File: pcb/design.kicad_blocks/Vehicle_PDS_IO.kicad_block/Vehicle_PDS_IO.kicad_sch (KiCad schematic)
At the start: 1 part, among them J10 FFC2B28-24-G

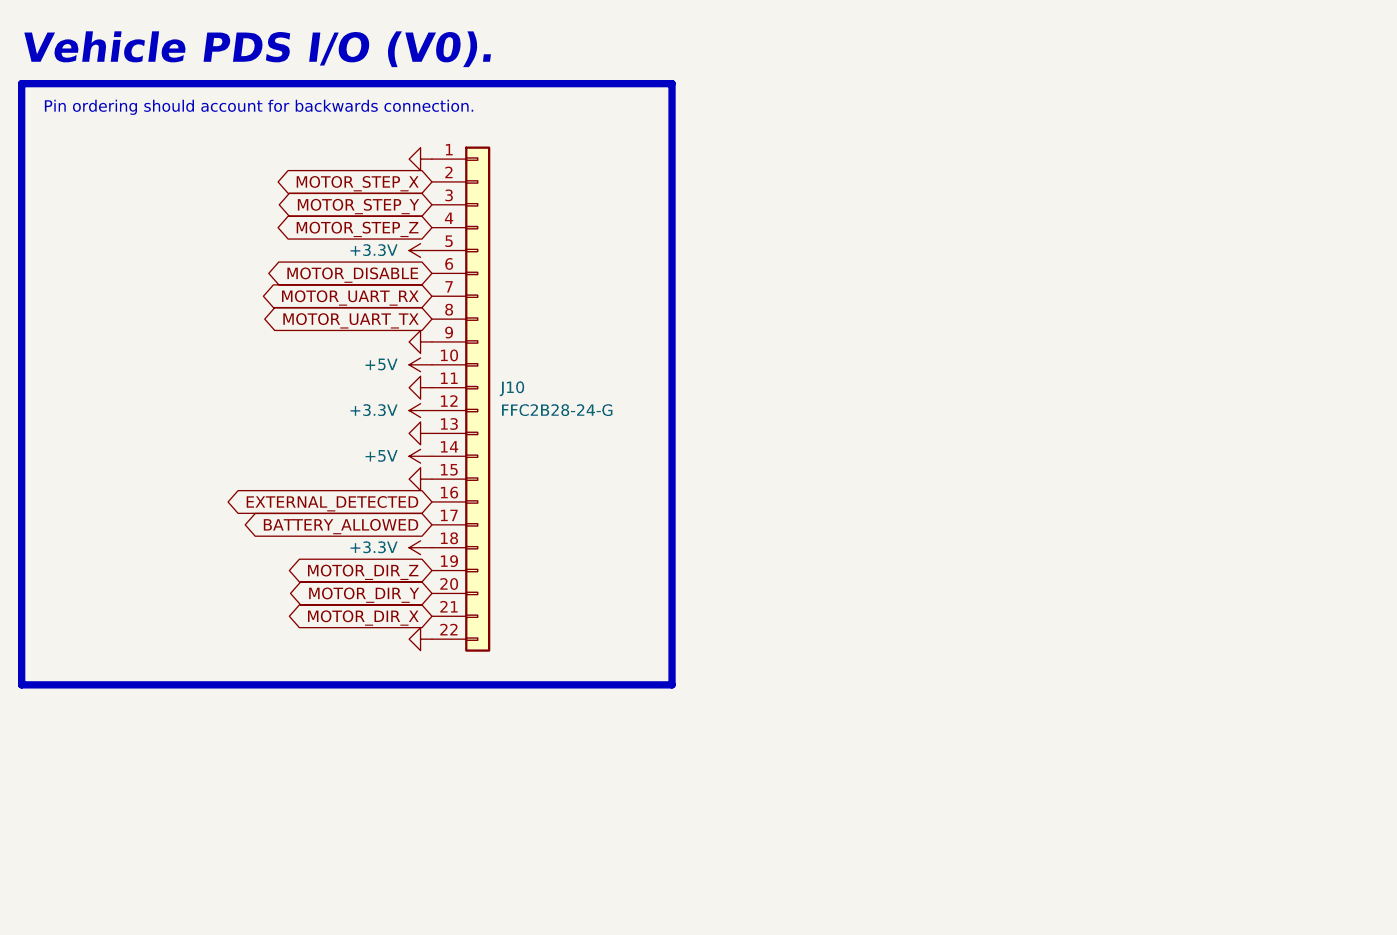
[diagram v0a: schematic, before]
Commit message: `Vehicle PDS I/O (V1 : Fixed pin-count).`
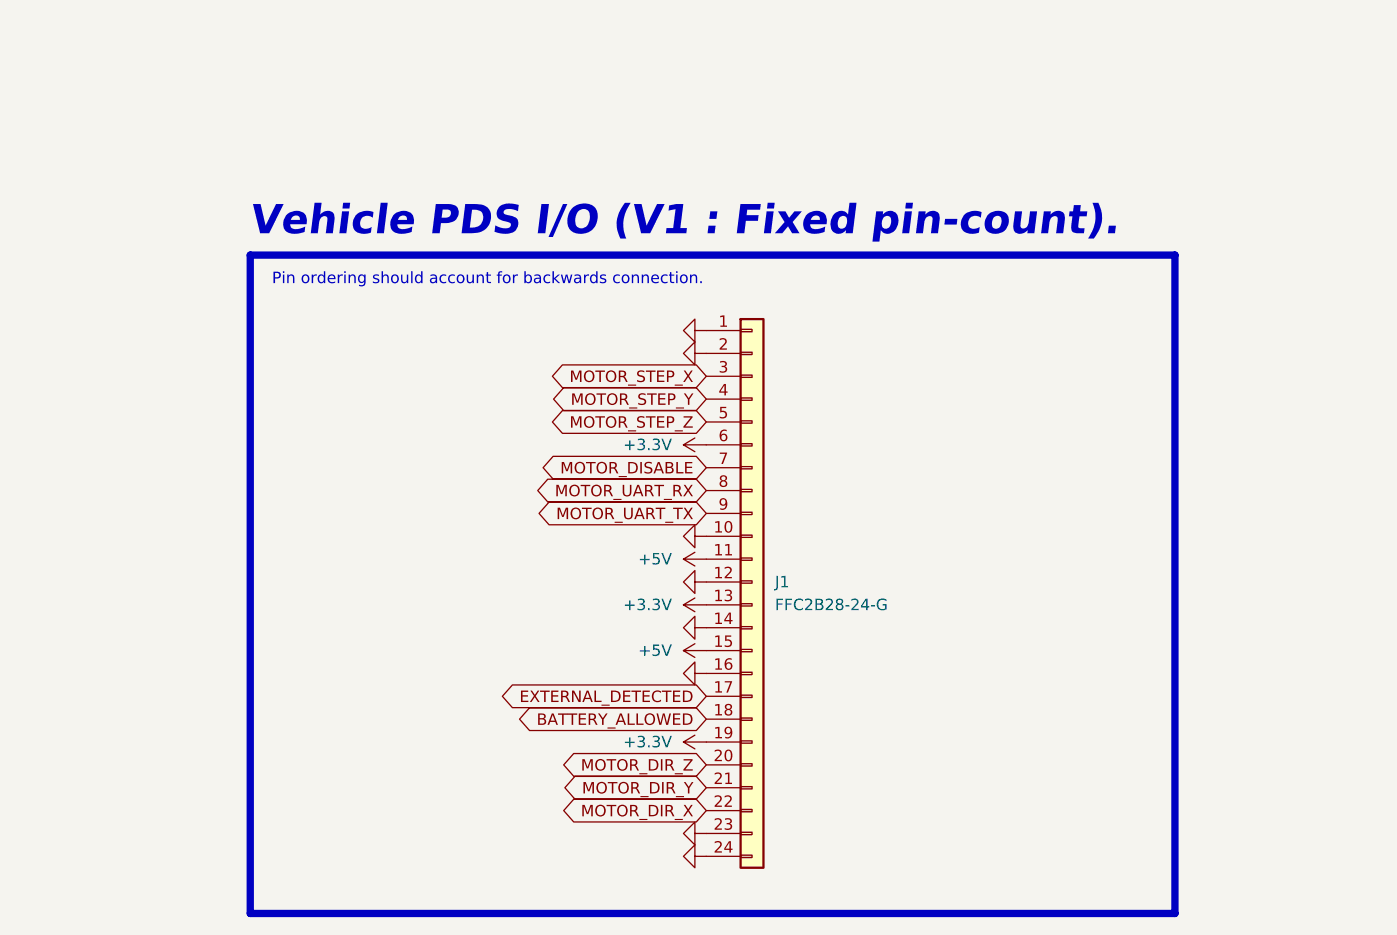
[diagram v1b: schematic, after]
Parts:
- J1: renamed from J10; symbol Connector_Generic:Conn_01x22 -> Connector_Generic:Conn_01x24
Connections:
- net +3.3V: now also J1.13 (Pin_13), J1.19 (Pin_19), J1.6 (Pin_6); no longer J1.12 (Pin_12), J1.18 (Pin_18), J1.5 (Pin_5)
- net +5V: now also J1.11 (Pin_11), J1.15 (Pin_15); no longer J1.10 (Pin_10), J1.14 (Pin_14)
- net BATTERY_ALLOWED: now also J1.18 (Pin_18); no longer J1.17 (Pin_17)
- net EXTERNAL_DETECTED: now also J1.17 (Pin_17); no longer J1.16 (Pin_16)
- net GND: now also J1.10 (Pin_10), J1.12 (Pin_12), J1.14 (Pin_14), J1.16 (Pin_16), J1.2 (Pin_2), J1.23 (Pin_23), J1.24 (Pin_24); no longer J1.11 (Pin_11), J1.13 (Pin_13), J1.15 (Pin_15), J1.22 (Pin_22), J1.9 (Pin_9)
- net MOTOR_DIR_X: now also J1.22 (Pin_22); no longer J1.21 (Pin_21)
- net MOTOR_DIR_Y: now also J1.21 (Pin_21); no longer J1.20 (Pin_20)
- net MOTOR_DIR_Z: now also J1.20 (Pin_20); no longer J1.19 (Pin_19)
- net MOTOR_DISABLE: now also J1.7 (Pin_7); no longer J1.6 (Pin_6)
- net MOTOR_STEP_X: now also J1.3 (Pin_3); no longer J1.2 (Pin_2)
- net MOTOR_STEP_Y: now also J1.4 (Pin_4); no longer J1.3 (Pin_3)
- net MOTOR_STEP_Z: now also J1.5 (Pin_5); no longer J1.4 (Pin_4)
- net MOTOR_UART_RX: now also J1.8 (Pin_8); no longer J1.7 (Pin_7)
- net MOTOR_UART_TX: now also J1.9 (Pin_9); no longer J1.8 (Pin_8)
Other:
- note added: "Vehicle PDS I/O (V1 : Fixed pin-count)."
- note removed: "Vehicle PDS I/O (V0)."

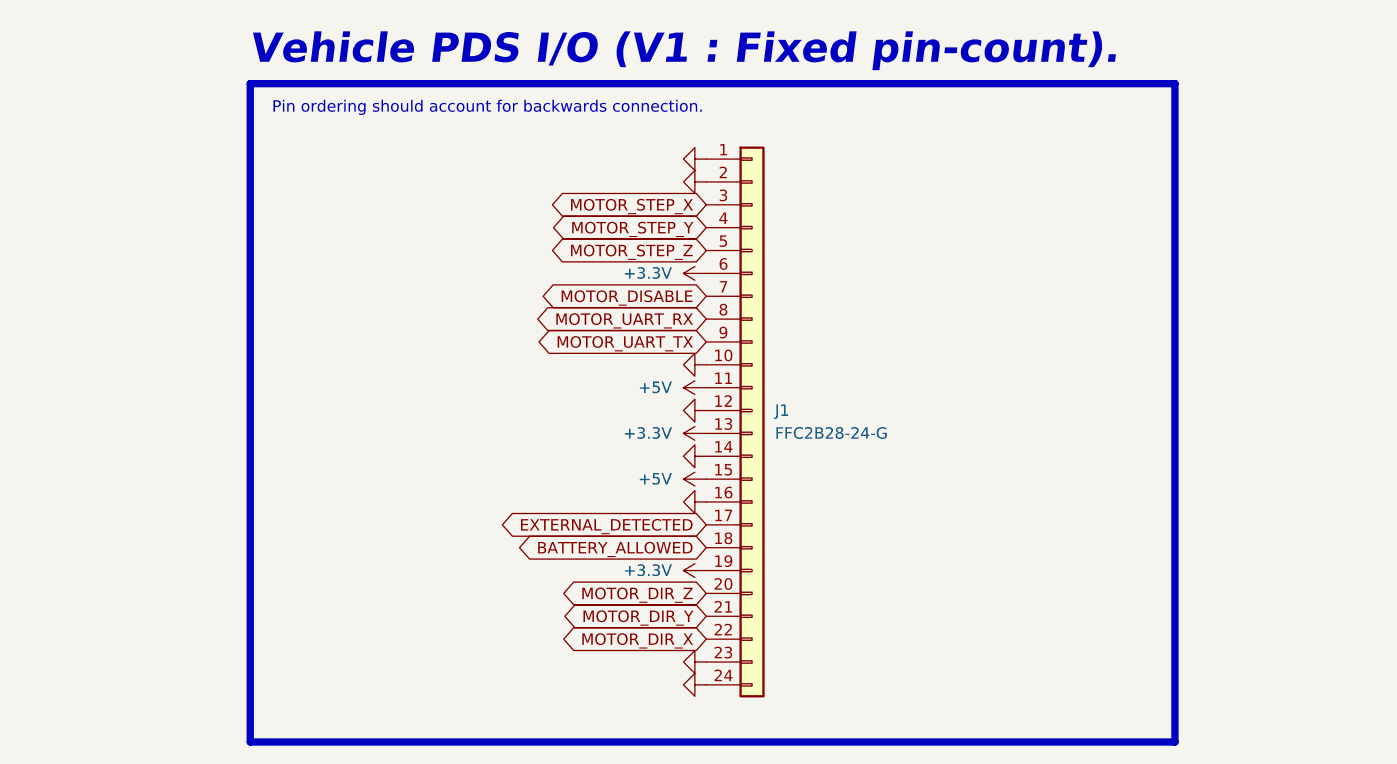
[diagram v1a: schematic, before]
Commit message: Made `VehicleFlightComputer` target and corrected nets for the STM32H533VET6 on `VehicleFlightComputer` PCB.
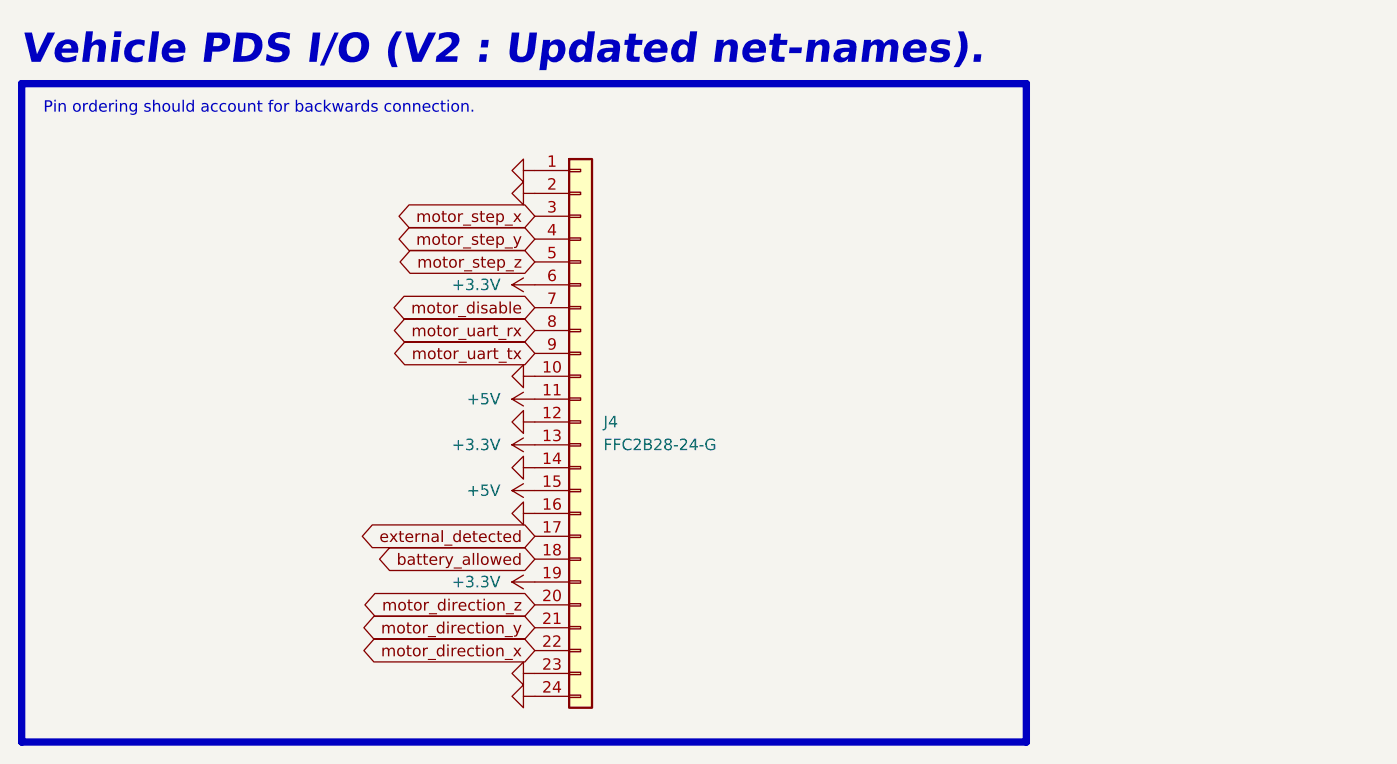
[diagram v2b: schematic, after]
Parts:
- renumbered J1 to J4
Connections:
- net BATTERY_ALLOWED renamed battery_allowed
- net EXTERNAL_DETECTED renamed external_detected
- net MOTOR_DIR_X renamed motor_direction_x
- net MOTOR_DIR_Y renamed motor_direction_y
- net MOTOR_DIR_Z renamed motor_direction_z
- net MOTOR_DISABLE renamed motor_disable
- net MOTOR_STEP_X renamed motor_step_x
- net MOTOR_STEP_Y renamed motor_step_y
- net MOTOR_STEP_Z renamed motor_step_z
- net MOTOR_UART_RX renamed motor_uart_rx
- net MOTOR_UART_TX renamed motor_uart_tx
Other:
- note added: "Vehicle PDS I/O (V2 : Updated net-names)."
- note removed: "Vehicle PDS I/O (V1 : Fixed pin-count)."
- moved on the sheet: J4

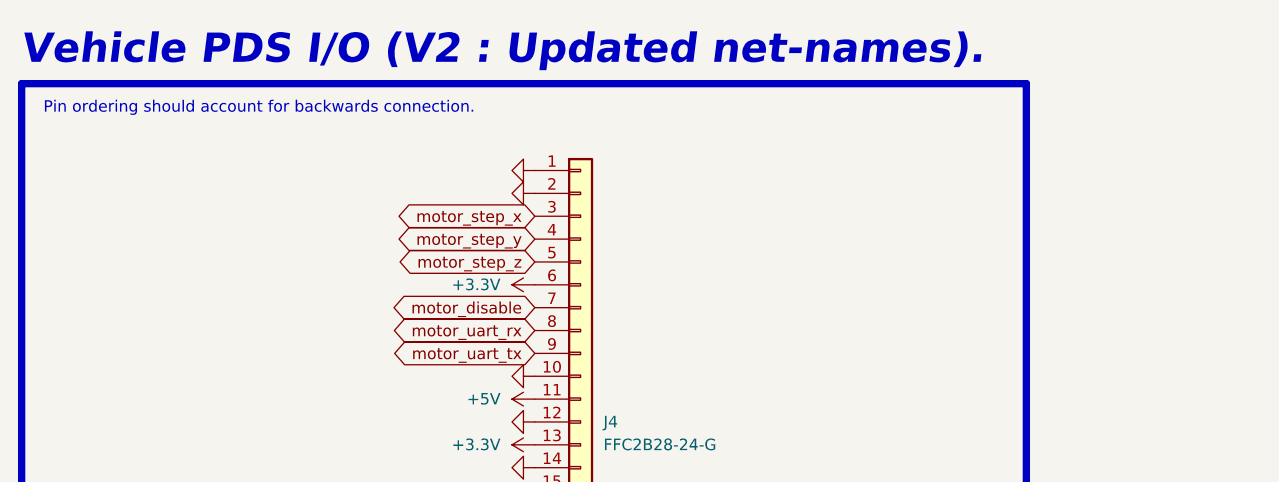
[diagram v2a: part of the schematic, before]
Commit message: Changed `motor_disable` to `motor_enable` in `VehicleFlightComputer` schematic.
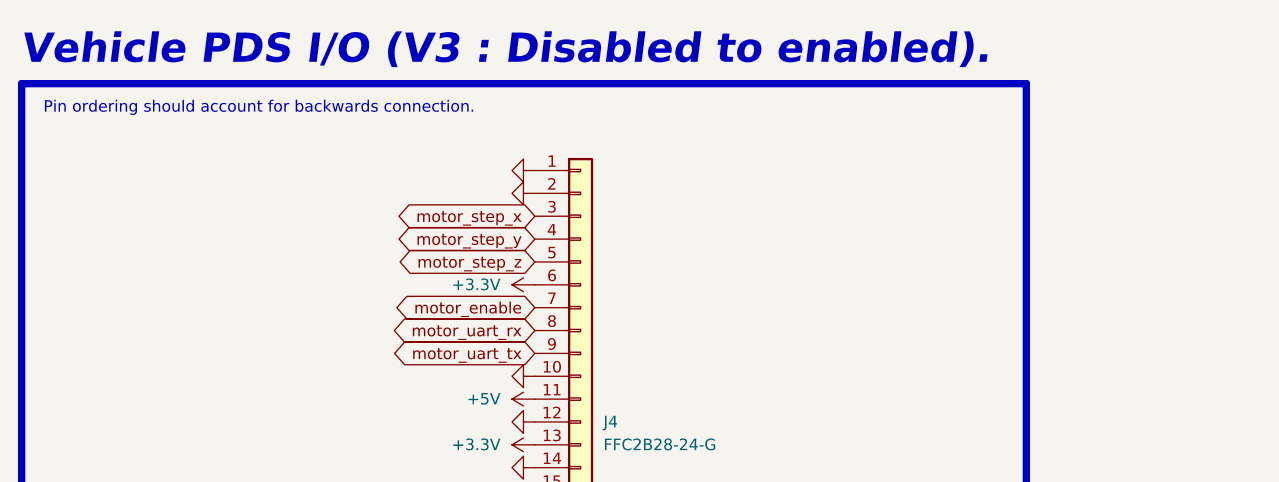
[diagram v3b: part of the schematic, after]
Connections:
- net motor_disable renamed motor_enable
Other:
- note added: "Vehicle PDS I/O (V3 : Disabled to enabled)."
- note removed: "Vehicle PDS I/O (V2 : Updated net-names)."
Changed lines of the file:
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@@
 		)
 	)
-	(text "Vehicle PDS I/O (V2 : Updated net-names)."
+	(text "Vehicle PDS I/O (V3 : Disabled to enabled)."
 		(exclude_from_sim no)
 		(at 463.55 297.18 0)
@@
 		)
 	)
-	(global_label "motor_disable"
+	(global_label "motor_enable"
 		(shape bidirectional)
 		(at 520.7 323.85 180)
@@
 		)
 		(property "Intersheetrefs" "${INTERSHEET_REFS}"
-			(at 503.299 323.85 0)
+			(at 503.8433 323.85 0)
 			(effects
 				(font
@@
 		(dnp no)
 		(fields_autoplaced yes)
-		(property "Reference" "#PWR070"
+		(property "Reference" "#PWR075"
 			(at 524.51 344.17 0)
 			(effects
@@
 			(project ""
 				(path "/378ff2fd-4011-4cd9-8b06-ddd39885e073"
-					(reference "#PWR070")
+					(reference "#PWR075")
 					(unit 1)
 				)
@@
 		(dnp no)
 		(fields_autoplaced yes)
-		(property "Reference" "#PWR066"
+		(property "Reference" "#PWR071"
 			(at 524.51 334.01 0)
 			(effects
@@
 			(project ""
 				(path "/378ff2fd-4011-4cd9-8b06-ddd39885e073"
-					(reference "#PWR066")
+					(reference "#PWR071")
 					(unit 1)
 				)
@@
 		(dnp no)
 		(fields_autoplaced yes)
-		(property "Reference" "#PWR063"
+		(property "Reference" "#PWR068"
 			(at 514.35 311.15 0)
 			(effects
@@
 			(project ""
 				(path "/378ff2fd-4011-4cd9-8b06-ddd39885e073"
-					(reference "#PWR063")
+					(reference "#PWR068")
 					(unit 1)
 				)
@@
 		(dnp no)
 		(fields_autoplaced yes)
-		(property "Reference" "#PWR071"
+		(property "Reference" "#PWR076"
 			(at 514.35 346.71 0)
 			(effects
@@
 			(project ""
 				(path "/378ff2fd-4011-4cd9-8b06-ddd39885e073"
-					(reference "#PWR071")
+					(reference "#PWR076")
 					(unit 1)
 				)
@@
 		(dnp no)
 		(fields_autoplaced yes)
-		(property "Reference" "#PWR065"
+		(property "Reference" "#PWR070"
 			(at 514.35 331.47 0)
 			(effects
@@
 			(project ""
 				(path "/378ff2fd-4011-4cd9-8b06-ddd39885e073"
-					(reference "#PWR065")
+					(reference "#PWR070")
 					(unit 1)
 				)
@@
 		(dnp no)
 		(fields_autoplaced yes)
-		(property "Reference" "#PWR072"
+		(property "Reference" "#PWR077"
 			(at 524.51 354.33 0)
 			(effects
@@
 			(project ""
 				(path "/378ff2fd-4011-4cd9-8b06-ddd39885e073"
-					(reference "#PWR072")
+					(reference "#PWR077")
 					(unit 1)
 				)
@@
 		(dnp no)
 		(fields_autoplaced yes)
-		(property "Reference" "#PWR067"
+		(property "Reference" "#PWR072"
 			(at 514.35 336.55 0)
 			(effects
@@
 			(project ""
 				(path "/378ff2fd-4011-4cd9-8b06-ddd39885e073"
-					(reference "#PWR067")
+					(reference "#PWR072")
 					(unit 1)
 				)
@@
 		(dnp no)
 		(fields_autoplaced yes)
-		(property "Reference" "#PWR073"
+		(property "Reference" "#PWR078"
 			(at 514.35 364.49 0)
 			(effects
@@
 			(project ""
 				(path "/378ff2fd-4011-4cd9-8b06-ddd39885e073"
-					(reference "#PWR073")
+					(reference "#PWR078")
 					(unit 1)
 				)
@@
 		(dnp no)
 		(fields_autoplaced yes)
-		(property "Reference" "#PWR062"
+		(property "Reference" "#PWR067"
 			(at 514.35 308.61 0)
 			(effects
@@
 			(project "VehicleFlightComputer"
 				(path "/378ff2fd-4011-4cd9-8b06-ddd39885e073"
-					(reference "#PWR062")
+					(reference "#PWR067")
 					(unit 1)
 				)
@@
 		(dnp no)
 		(fields_autoplaced yes)
-		(property "Reference" "#PWR064"
+		(property "Reference" "#PWR069"
 			(at 524.51 321.31 0)
 			(effects
@@
 			(project ""
 				(path "/378ff2fd-4011-4cd9-8b06-ddd39885e073"
-					(reference "#PWR064")
+					(reference "#PWR069")
 					(unit 1)
 				)
@@
 		(dnp no)
 		(fields_autoplaced yes)
-		(property "Reference" "#PWR068"
+		(property "Reference" "#PWR073"
 			(at 524.51 339.09 0)
 			(effects
@@
 			(project ""
 				(path "/378ff2fd-4011-4cd9-8b06-ddd39885e073"
-					(reference "#PWR068")
+					(reference "#PWR073")
 					(unit 1)
 				)
@@
 		(dnp no)
 		(fields_autoplaced yes)
-		(property "Reference" "#PWR074"
+		(property "Reference" "#PWR079"
 			(at 514.35 367.03 0)
 			(effects
@@
 			(project "VehicleFlightComputer"
 				(path "/378ff2fd-4011-4cd9-8b06-ddd39885e073"
-					(reference "#PWR074")
+					(reference "#PWR079")
 					(unit 1)
 				)
@@
 		(dnp no)
 		(fields_autoplaced yes)
-		(property "Reference" "#PWR069"
+		(property "Reference" "#PWR074"
 			(at 514.35 341.63 0)
 			(effects
@@
 			(project ""
 				(path "/378ff2fd-4011-4cd9-8b06-ddd39885e073"
-					(reference "#PWR069")
-					(unit 1)
-				)
+					(reference "#PWR074")
+					(unit 1)
+				)
